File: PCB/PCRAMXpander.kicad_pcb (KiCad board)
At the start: 2 copper layers, 134.6 x 97.8 mm, 22 parts, among them J1 Bus_ISA_16bit, U1 ATF16V8B-15PU, U2 SN74LVCR16245ADGGR, U3 SN74LVC16244ADGGR, U4 SN74LVC16244ADGGR, U5 AS6C3216A-55TIN, U6 AS6C3216A-55TIN

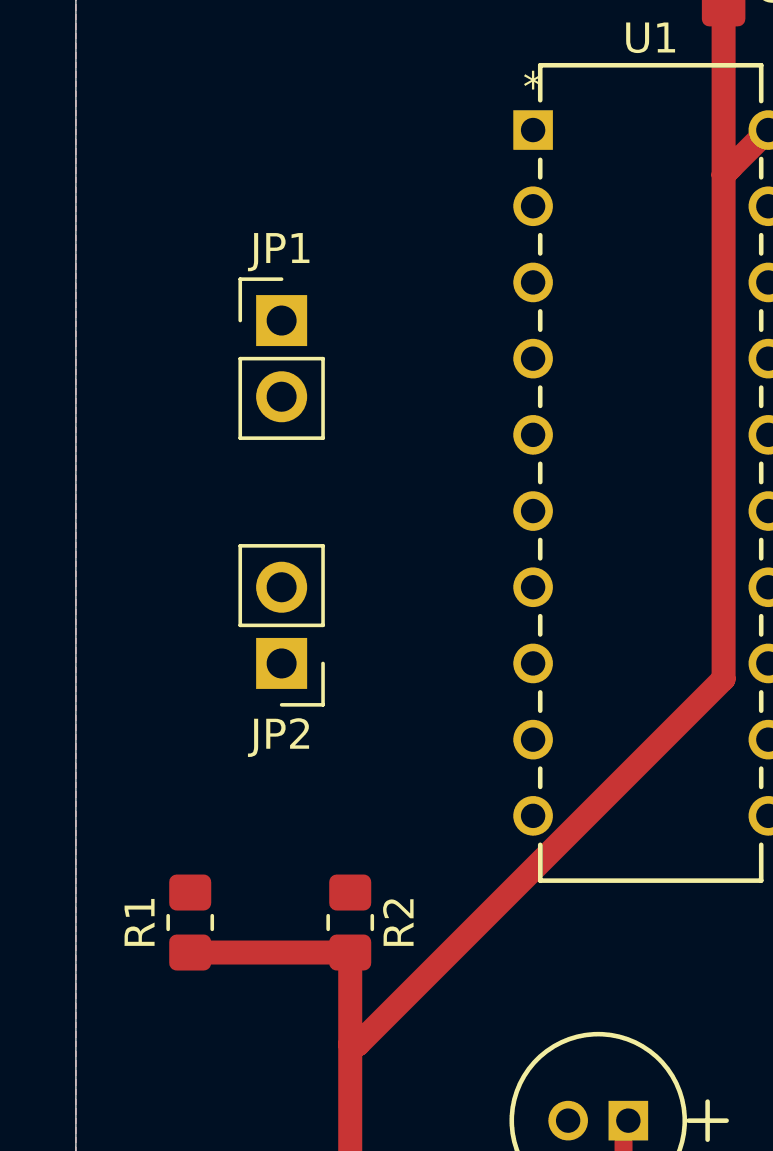
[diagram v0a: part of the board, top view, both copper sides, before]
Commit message: 5v refinement
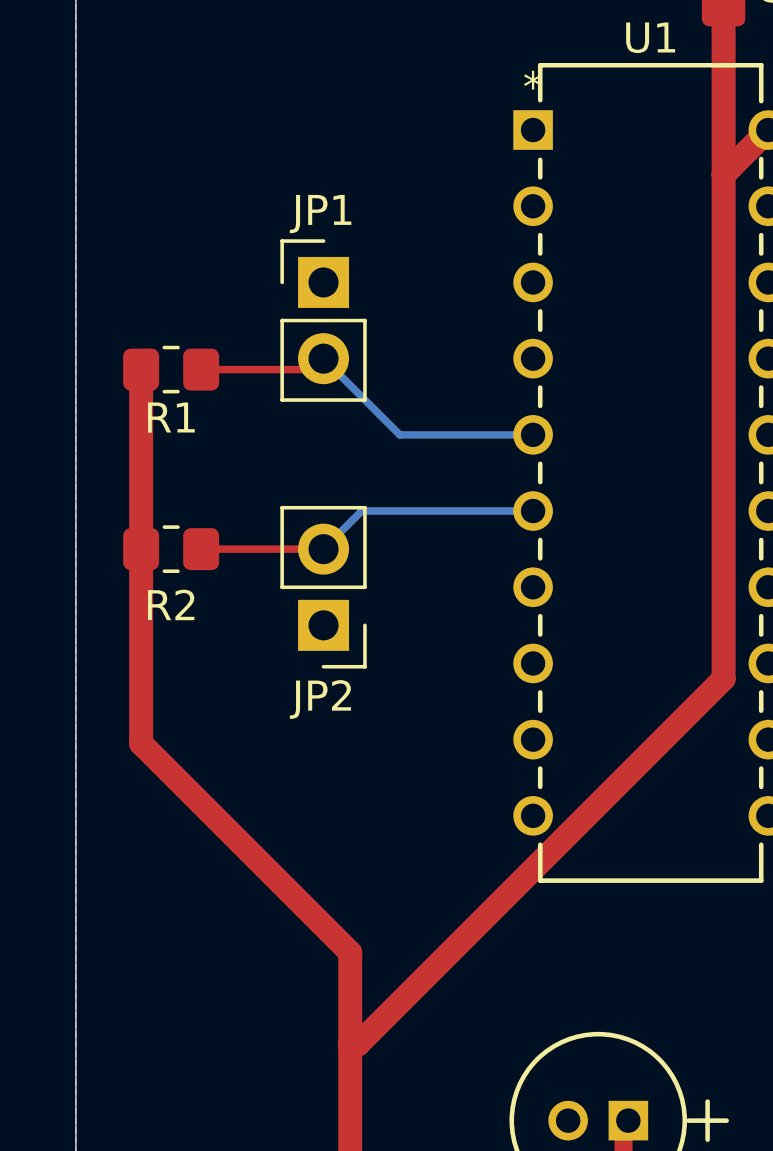
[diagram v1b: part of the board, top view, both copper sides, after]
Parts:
- moved R1 18.4 mm to (66.7, 99.4), turned to 0 degrees
- moved R2 13.8 mm to (66.7, 105.4), turned to 180 degrees
- moved JP1 1.89 mm to (71.8, 96.5)
- moved JP2 1.89 mm to (71.8, 108.0)
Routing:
- net +5V: track 221.4 -> 238.3 mm
- net Net-(JP1-B): track 0.00 -> 12.3 mm
- net Net-(JP2-B): track 0.00 -> 11.6 mm
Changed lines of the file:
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@@
 	(footprint "Resistor_SMD:R_0805_2012Metric_Pad1.20x1.40mm_HandSolder"
 		(layer "F.Cu")
-		(at 72.644 117.856 -90)
+		(at 66.675 105.41 180)
 		(descr "Resistor SMD 0805 (2012 Metric), square (rectangular) end terminal, IPC-7351 nominal with elongated pad for handsoldering. (Body size source: IPC-SM-782 page 72, https://www.pcb-3d.com/wordpress/wp-content/uploads/ipc-sm-782a_amendment_1_and_2.pdf), generated with kicad-footprint-generator")
 		(tags "resistor handsolder")
 		(property "Reference" "R2"
-			(at 0 -1.65 90)
+			(at 0 -1.905 0)
 			(layer "F.SilkS")
 			(effects
@@
 		)
 		(property "Value" "10k"
-			(at 0 1.65 90)
+			(at 0 1.65 0)
 			(layer "F.Fab")
 			(effects
@@
 		)
 		(property "Datasheet" "~"
-			(at 0 0 90)
+			(at 0 0 0)
 			(layer "F.Fab")
 			(hide yes)
@@
 		)
 		(property "Description" "Resistor"
-			(at 0 0 90)
+			(at 0 0 0)
 			(layer "F.Fab")
 			(hide yes)
@@
 		)
 		(fp_line
-			(start -1.85 0.95)
-			(end -1.85 -0.95)
+			(start 1.85 0.95)
+			(end -1.85 0.95)
 			(stroke
 				(width 0.05)
@@
 		)
 		(fp_line
-			(start 1.85 0.95)
-			(end -1.85 0.95)
+			(start 1.85 -0.95)
+			(end 1.85 0.95)
 			(stroke
 				(width 0.05)
@@
 		)
 		(fp_line
-			(start -1.85 -0.95)
-			(end 1.85 -0.95)
+			(start -1.85 0.95)
+			(end -1.85 -0.95)
 			(stroke
 				(width 0.05)
@@
 		)
 		(fp_line
-			(start 1.85 -0.95)
-			(end 1.85 0.95)
+			(start -1.85 -0.95)
+			(end 1.85 -0.95)
 			(stroke
 				(width 0.05)
@@
 		)
 		(fp_line
-			(start -1 0.625)
-			(end -1 -0.625)
+			(start 1 0.625)
+			(end -1 0.625)
 			(stroke
 				(width 0.1)
@@
 		)
 		(fp_line
-			(start 1 0.625)
-			(end -1 0.625)
+			(start 1 -0.625)
+			(end 1 0.625)
 			(stroke
 				(width 0.1)
@@
 		)
 		(fp_line
-			(start -1 -0.625)
-			(end 1 -0.625)
+			(start -1 0.625)
+			(end -1 -0.625)
 			(stroke
 				(width 0.1)
@@
 		)
 		(fp_line
-			(start 1 -0.625)
-			(end 1 0.625)
+			(start -1 -0.625)
+			(end 1 -0.625)
 			(stroke
 				(width 0.1)
@@
 		)
 		(fp_text user "${REFERENCE}"
-			(at 0 0 90)
+			(at 0 0 0)
 			(layer "F.Fab")
 			(effects
@@
 		)
 		(pad "1" smd roundrect
-			(at -1 0 270)
+			(at -1 0 180)
 			(size 1.2 1.4)
 			(layers "F.Cu" "F.Mask" "F.Paste")
@@
 		)
 		(pad "2" smd roundrect
-			(at 1 0 270)
+			(at 1 0 180)
 			(size 1.2 1.4)
 			(layers "F.Cu" "F.Mask" "F.Paste")
@@
 	(footprint "Resistor_SMD:R_0805_2012Metric_Pad1.20x1.40mm_HandSolder"
 		(layer "F.Cu")
-		(at 67.31 117.856 90)
+		(at 66.675 99.425)
 		(descr "Resistor SMD 0805 (2012 Metric), square (rectangular) end terminal, IPC-7351 nominal with elongated pad for handsoldering. (Body size source: IPC-SM-782 page 72, https://www.pcb-3d.com/wordpress/wp-content/uploads/ipc-sm-782a_amendment_1_and_2.pdf), generated with kicad-footprint-generator")
 		(tags "resistor handsolder")
 		(property "Reference" "R1"
-			(at 0 -1.65 90)
+			(at 0 1.635 0)
 			(layer "F.SilkS")
 			(effects
@@
 		)
 		(property "Value" "10k"
-			(at 0 1.65 90)
+			(at 0 1.65 0)
 			(layer "F.Fab")
 			(effects
@@
 		)
 		(property "Datasheet" "~"
-			(at 0 0 90)
+			(at 0 0 0)
 			(layer "F.Fab")
 			(hide yes)
@@
 		)
 		(property "Description" "Resistor"
-			(at 0 0 90)
+			(at 0 0 0)
 			(layer "F.Fab")
 			(hide yes)
@@
 		)
 		(fp_line
-			(start 1.85 -0.95)
-			(end 1.85 0.95)
+			(start -1.85 -0.95)
+			(end 1.85 -0.95)
 			(stroke
 				(width 0.05)
@@
 		)
 		(fp_line
-			(start -1.85 -0.95)
-			(end 1.85 -0.95)
+			(start -1.85 0.95)
+			(end -1.85 -0.95)
 			(stroke
 				(width 0.05)
@@
 		)
 		(fp_line
-			(start 1.85 0.95)
-			(end -1.85 0.95)
+			(start 1.85 -0.95)
+			(end 1.85 0.95)
 			(stroke
 				(width 0.05)
@@
 		)
 		(fp_line
-			(start -1.85 0.95)
-			(end -1.85 -0.95)
+			(start 1.85 0.95)
+			(end -1.85 0.95)
 			(stroke
 				(width 0.05)
@@
 		)
 		(fp_line
-			(start 1 -0.625)
-			(end 1 0.625)
+			(start -1 -0.625)
+			(end 1 -0.625)
 			(stroke
 				(width 0.1)
@@
 		)
 		(fp_line
-			(start -1 -0.625)
-			(end 1 -0.625)
+			(start -1 0.625)
+			(end -1 -0.625)
 			(stroke
 				(width 0.1)
@@
 		)
 		(fp_line
-			(start 1 0.625)
-			(end -1 0.625)
+			(start 1 -0.625)
+			(end 1 0.625)
 			(stroke
 				(width 0.1)
@@
 		)
 		(fp_line
-			(start -1 0.625)
-			(end -1 -0.625)
+			(start 1 0.625)
+			(end -1 0.625)
 			(stroke
 				(width 0.1)
@@
 		)
 		(fp_text user "${REFERENCE}"
-			(at 0 0 90)
+			(at 0 0 0)
 			(layer "F.Fab")
 			(effects
@@
 		)
 		(pad "1" smd roundrect
-			(at -1 0 90)
+			(at -1 0)
 			(size 1.2 1.4)
 			(layers "F.Cu" "F.Mask" "F.Paste")
@@
 		)
 		(pad "2" smd roundrect
-			(at 1 0 90)
+			(at 1 0)
 			(size 1.2 1.4)
 			(layers "F.Cu" "F.Mask" "F.Paste")
@@
 	(footprint "Connector_PinHeader_2.54mm:PinHeader_1x02_P2.54mm_Vertical"
 		(layer "F.Cu")
-		(at 70.358 109.22 180)
+		(at 71.755 107.95 180)
 		(descr "Through hole straight pin header, 1x02, 2.54mm pitch, single row")
 		(tags "Through hole pin header THT 1x02 2.54mm single row")
@@
 	(footprint "Connector_PinHeader_2.54mm:PinHeader_1x02_P2.54mm_Vertical"
 		(layer "F.Cu")
-		(at 70.358 97.79)
+		(at 71.755 96.52)
 		(descr "Through hole straight pin header, 1x02, 2.54mm pitch, single row")
 		(tags "Through hole pin header THT 1x02 2.54mm single row")
@@
 	)
 	(segment
+		(start 65.675 111.887)
+		(end 65.675 105.41)
+		(width 0.8)
+		(layer "F.Cu")
+		(net 53)
+	)
+	(segment
 		(start 75.725 135.65)
 		(end 72.644 132.569)
@@
 	)
 	(segment
+		(start 65.675 105.41)
+		(end 65.675 99.425)
+		(width 0.8)
+		(layer "F.Cu")
+		(net 53)
+	)
+	(segment
 		(start 72.903889 121.92)
 		(end 85.09 109.733889)
@@
 	)
 	(segment
-		(start 71.12 140.255)
-		(end 75.725 135.65)
+		(start 72.644 118.856)
+		(end 65.675 111.887)
 		(width 0.8)
 		(layer "F.Cu")
@@
 	)
 	(segment
-		(start 72.644 121.92)
-		(end 72.644 118.856)
+		(start 71.12 140.255)
+		(end 75.725 135.65)
 		(width 0.8)
 		(layer "F.Cu")
@@
 	)
 	(segment
-		(start 67.31 118.856)
-		(end 72.644 118.856)
-		(width 0.8)
-		(layer "F.Cu")
-		(net 53)
-	)
-	(segment
 		(start 72.644 121.92)
 		(end 72.903889 121.92)
@@
 	)
 	(segment
+		(start 72.644 121.92)
+		(end 72.644 118.856)
+		(width 0.8)
+		(layer "F.Cu")
+		(net 53)
+	)
+	(segment
 		(start 85.09 92.932001)
 		(end 85.320601 92.7014)
@@
 	)
 	(segment
+		(start 67.675 99.425)
+		(end 71.39 99.425)
+		(width 0.25)
+		(layer "F.Cu")
+		(net 93)
+	)
+	(segment
+		(start 71.39 99.425)
+		(end 71.755 99.06)
+		(width 0.25)
+		(layer "F.Cu")
+		(net 93)
+	)
+	(segment
+		(start 71.755 99.06)
+		(end 74.295 101.6)
+		(width 0.25)
+		(layer "B.Cu")
+		(net 93)
+	)
+	(segment
+		(start 74.295 101.6)
+		(end 78.74 101.6)
+		(width 0.25)
+		(layer "B.Cu")
+		(net 93)
+	)
+	(segment
+		(start 67.675 105.41)
+		(end 71.755 105.41)
+		(width 0.25)
+		(layer "F.Cu")
+		(net 94)
+	)
+	(segment
+		(start 71.755 105.41)
+		(end 73.025 104.14)
+		(width 0.25)
+		(layer "B.Cu")
+		(net 94)
+	)
+	(segment
+		(start 73.025 104.14)
+		(end 78.74 104.14)
+		(width 0.25)
+		(layer "B.Cu")
+		(net 94)
+	)
+	(segment

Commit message: SIP5 resistor pack
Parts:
- R3: value 10 kOhm -> 10k; footprint Project:RESCAV80P400X210X65-10N -> Project:CSC05_VIS
- moved C5 24.4 mm to (149.9, 97.2), turned to 0 degrees
- moved C6 22.5 mm to (153.0, 73.0), turned to 0 degrees
- moved JP3 15.2 mm to (177.8, 106.7)
- moved R3 8.08 mm to (116.2, 80.0), turned to 90 degrees
- moved U6 3.92 mm to (144.1, 87.0)
- moved U5 2.74 mm to (155.6, 63.5)
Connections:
- R3 pad 2: unconnected-(R3-Pad2) -> C2E
- R3 pad 4: unconnected-(R3-Pad4) -> WE
- R3 pad 5: unconnected-(R3-Pad5) -> C1E
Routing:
- net +3.3V: track 15.0 -> 380.4 mm, vias 0 -> 13
- net Net-(JP3-A): track 0.00 -> 91.2 mm

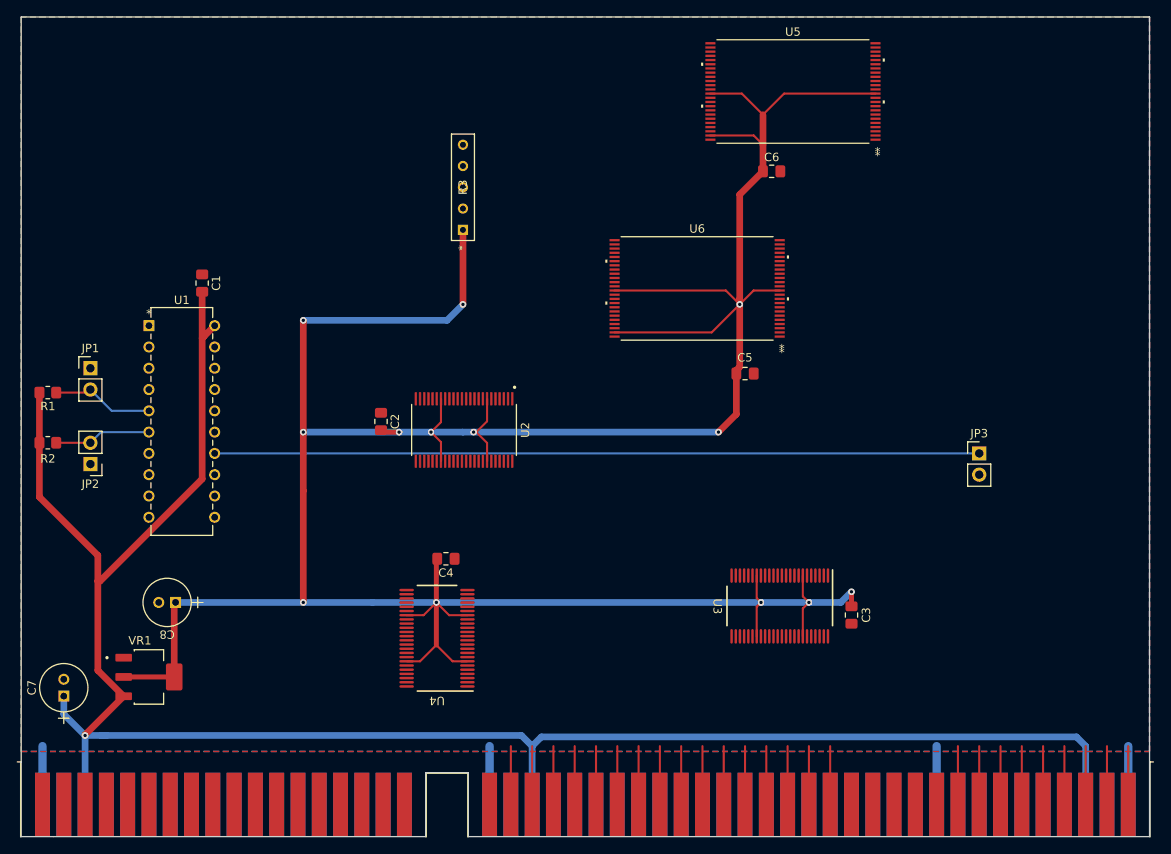
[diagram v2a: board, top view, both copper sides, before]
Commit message: Power refinement, ISA fingers
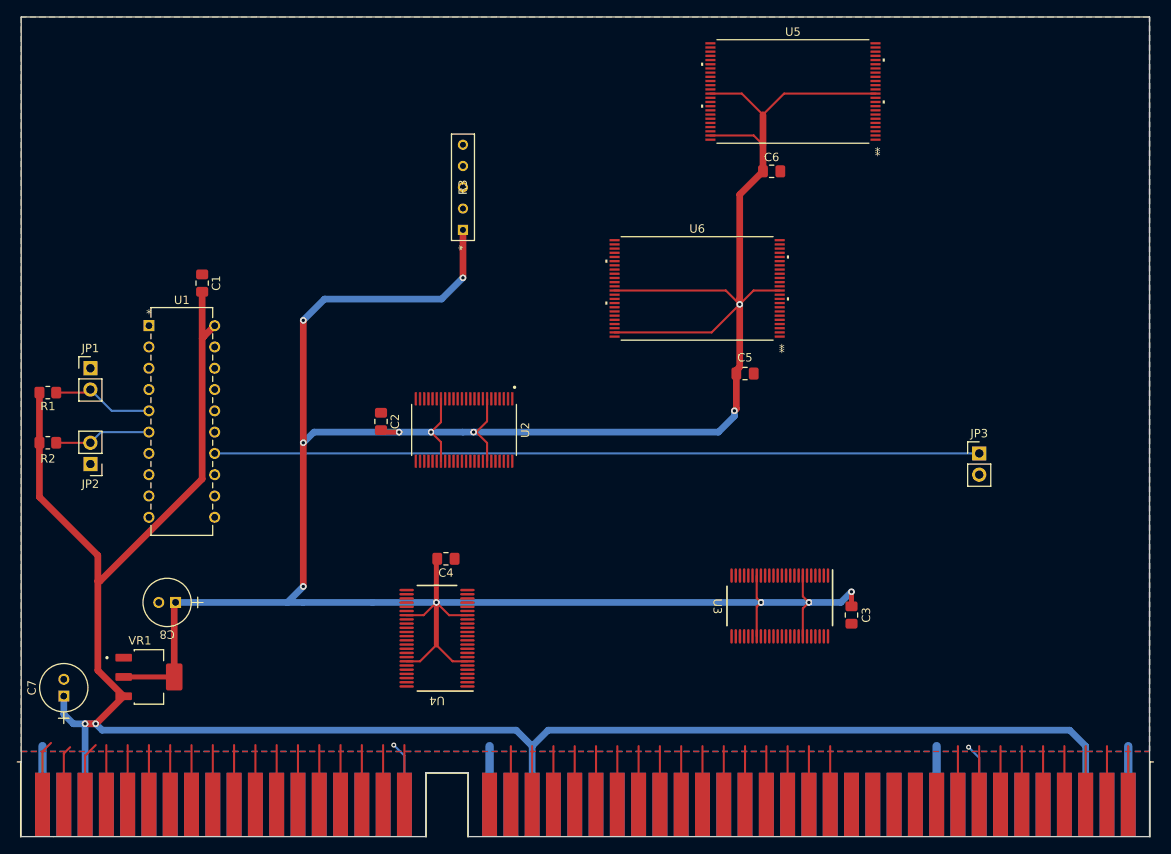
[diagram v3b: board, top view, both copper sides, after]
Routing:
- net Net-(J1-D15): track 0.00 -> 7.79 mm
- net Net-(J1-D13): track 0.00 -> 7.64 mm
- net MEMCS16: track 0.00 -> 7.64 mm, vias 0 -> 1
- net Net-(J1-NOWS): track 0.00 -> 7.38 mm, vias 0 -> 1
- net Net-(J1-D14): track 0.00 -> 7.17 mm
- net SBHE: track 0.00 -> 7.11 mm
- net Net-(J1-D9): track 0.00 -> 7.11 mm
- net Net-(J1-D8): track 0.00 -> 7.11 mm
- net Net-(J1-D12): track 0.00 -> 7.11 mm
- net Net-(J1-D11): track 0.00 -> 7.11 mm
- net Net-(J1-D10): track 0.00 -> 7.11 mm
- net MEMW: track 0.00 -> 7.11 mm
- net MEMR: track 0.00 -> 7.11 mm
- net LA23: track 0.00 -> 7.11 mm
- net LA22: track 0.00 -> 7.11 mm
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
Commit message: Power refinement
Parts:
- moved C5 14.0 mm to (135.9, 98.6)
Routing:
- net Net-(J1-D15): track 7.79 -> 80.2 mm, vias 0 -> 2
- net A1: track 0.00 -> 28.8 mm
- net +3.3V: track 379.9 -> 367.0 mm, vias 13 -> 21
- net OE: track 0.00 -> 6.25 mm
- net D2: track 0.00 -> 4.40 mm
- net D12: track 0.00 -> 4.37 mm
- net D13: track 0.00 -> 4.35 mm
- net D5: track 0.00 -> 4.29 mm
- net D4: track 0.00 -> 4.16 mm
- net D0: track 0.00 -> 4.15 mm
- net D6: track 0.00 -> 4.04 mm
- net D10: track 0.00 -> 4.04 mm
- net D1: track 0.00 -> 4.03 mm
- net TRANS_EN: track 0.00 -> 3.97 mm
- net D3: track 0.00 -> 3.95 mm
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
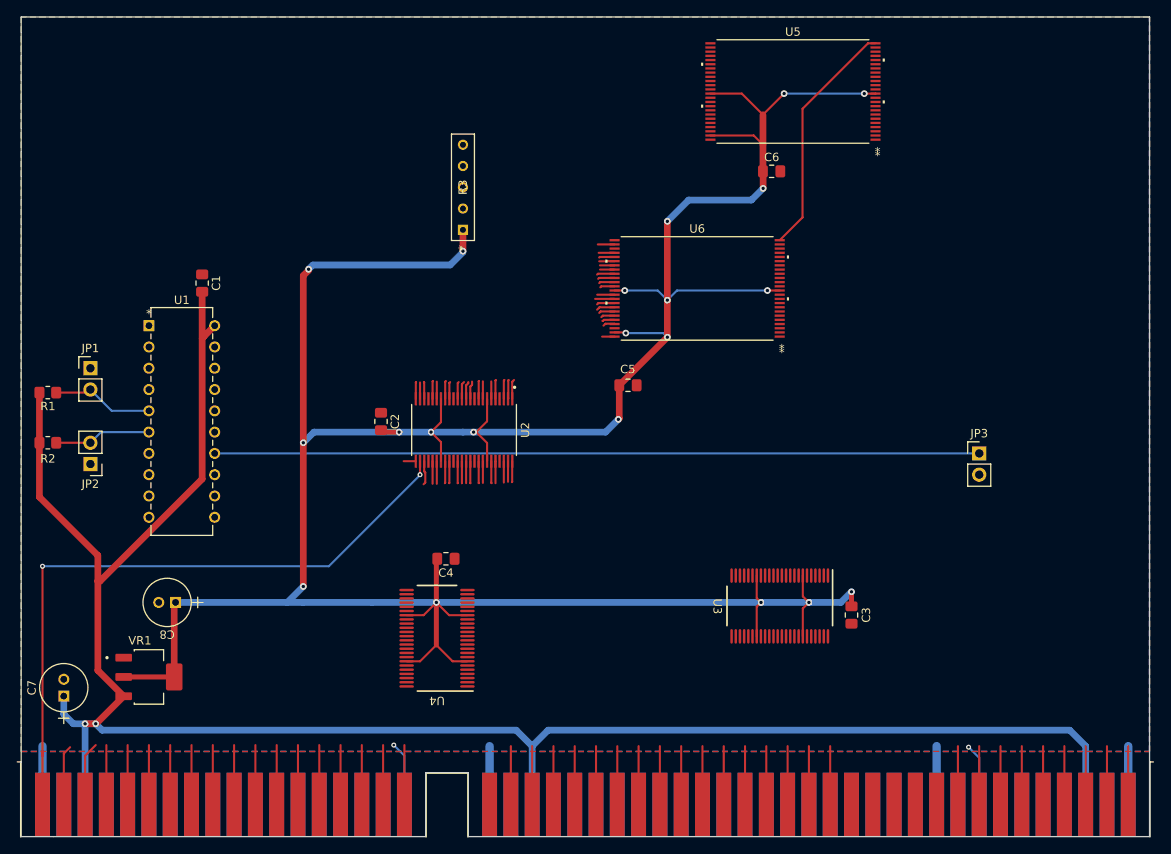
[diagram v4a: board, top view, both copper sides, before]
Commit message: U6 routing
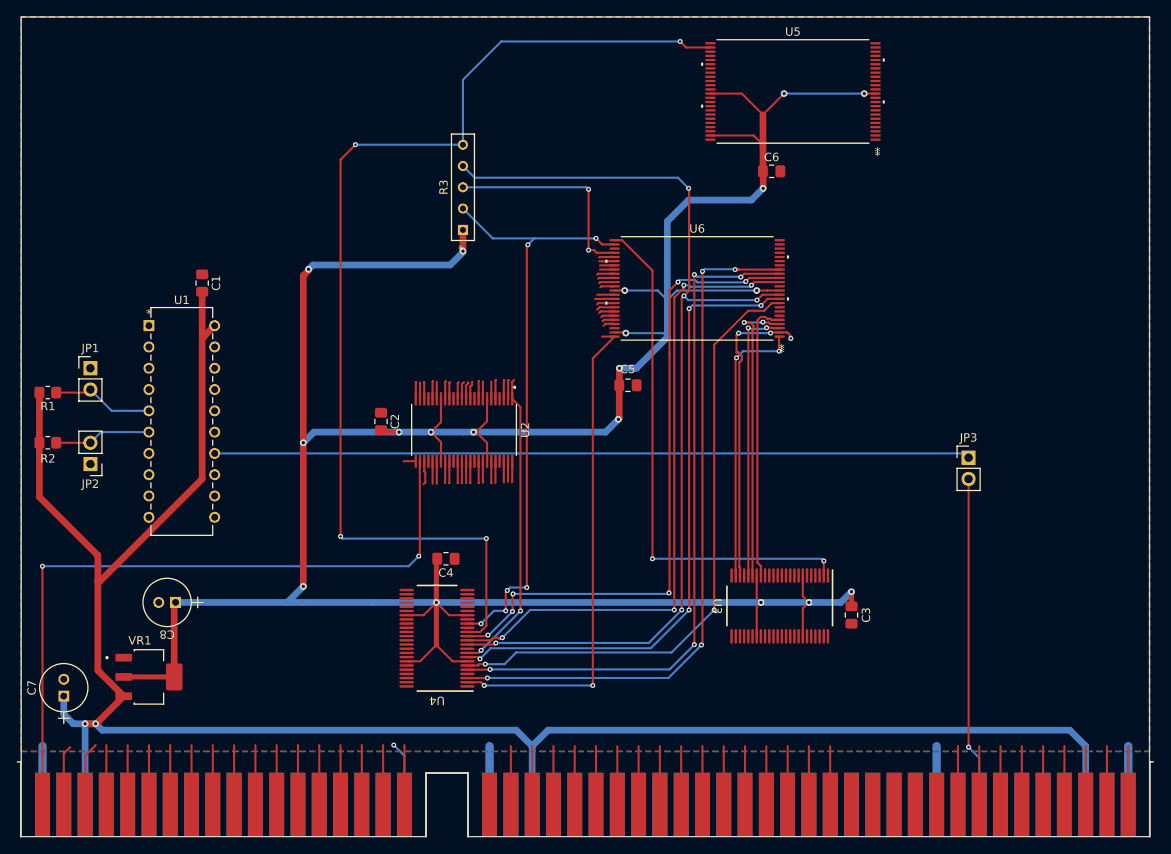
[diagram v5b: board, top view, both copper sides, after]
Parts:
- moved JP3 1.37 mm to (176.5, 107.2)
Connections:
- R3 pad 3: unconnected-(R3-Pad3) -> OE
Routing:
- net C1E: track 0.00 -> 130.2 mm, vias 0 -> 4
- net WE: track 0.00 -> 117.9 mm, vias 0 -> 5
- net A17: track 0.00 -> 83.6 mm, vias 0 -> 4
- net A18: track 0.00 -> 83.2 mm, vias 0 -> 4
- net LB: track 0.00 -> 77.5 mm, vias 0 -> 6
- net UB: track 0.00 -> 77.2 mm, vias 0 -> 4
- net A20: track 0.00 -> 76.3 mm, vias 0 -> 4
- net A19: track 0.00 -> 73.7 mm, vias 0 -> 2
- net C2E: track 2.01 -> 72.1 mm, vias 0 -> 6
- net A0: track 0.00 -> 62.8 mm, vias 0 -> 2
- net A16: track 1.49 -> 59.3 mm, vias 0 -> 2
- net OE: track 6.25 -> 64.0 mm, vias 0 -> 4
- net A14: track 0.00 -> 36.3 mm, vias 0 -> 3
- net A12: track 0.00 -> 35.5 mm, vias 0 -> 2
- net A11: track 0.00 -> 33.7 mm
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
